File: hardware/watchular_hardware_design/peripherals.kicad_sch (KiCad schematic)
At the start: 43 parts, among them Q1 BSS123, Q2 BSS123, Q3 BSS123, Q4 BSS123

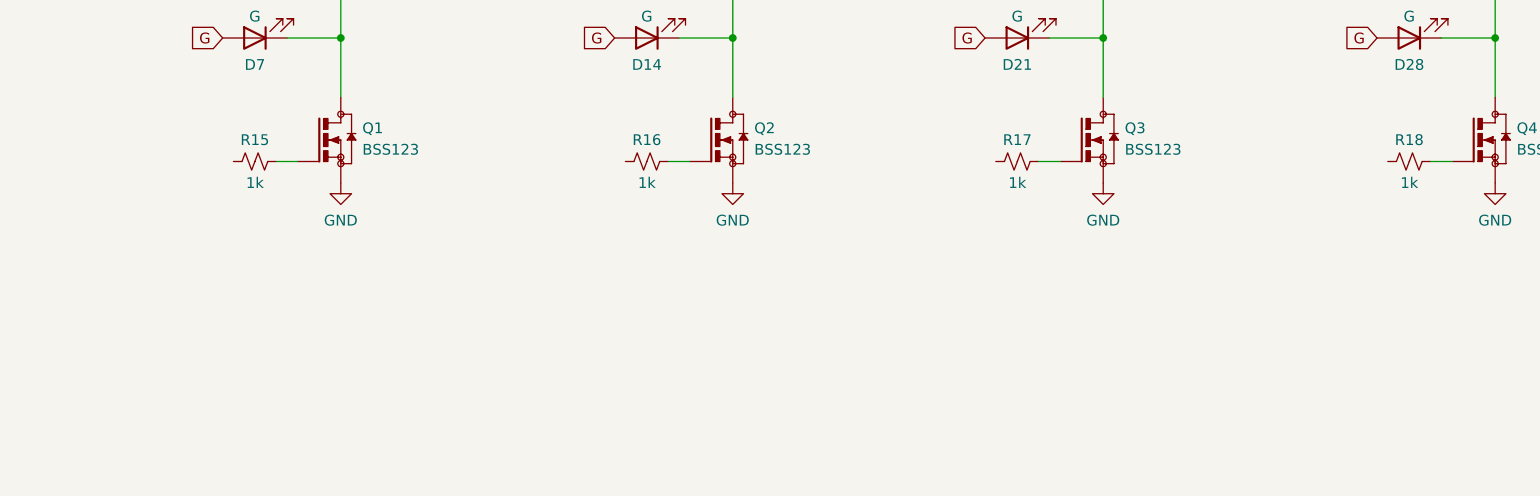
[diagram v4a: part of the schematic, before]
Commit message: Imported button library.
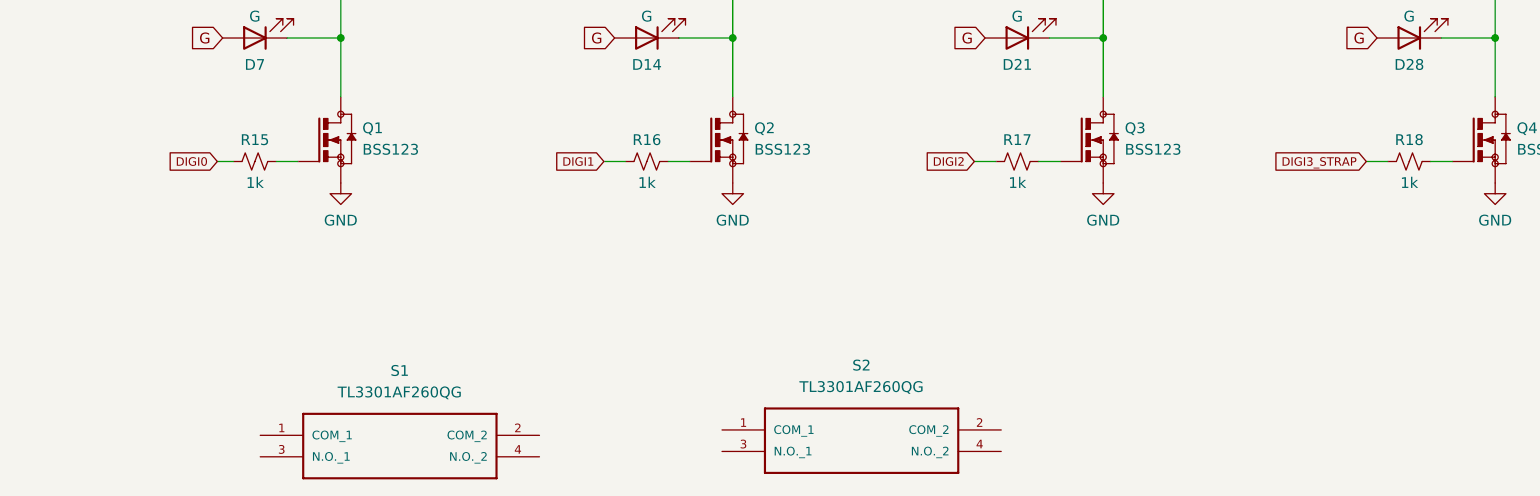
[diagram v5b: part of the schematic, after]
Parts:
- added S1, S2: TL3301AF260QG, switch-TL3301AF260QG:TL3301AF260QG, symbol TL3301AF260QG:TL3301AF260QG
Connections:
- net DIGI0: now reaches R15.1
- net DIGI2: now reaches R17.1
- net DIGI3_STRAP: now reaches R18.1
- net DIGI1: now reaches R16.1
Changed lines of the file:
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@@
+    (stroke (width 0) (type default) (color 0 0 0 0))
+  )
+  (wire (pts (xy 211.455 85.725) (xy 213.995 85.725))
     (stroke (width 0) (type default) (color 0 0 0 0))
   )
@@
     (stroke (width 0) (type default) (color 0 0 0 0))
   )
+  (wire (pts (xy 75.565 85.725) (xy 77.47 85.725))
+    (stroke (width 0) (type default) (color 0 0 0 0))
+  )
   (wire (pts (xy 130.175 45.085) (xy 136.525 45.085))
     (stroke (width 0) (type default) (color 0 0 0 0))
@@
     (stroke (width 0) (type default) (color 0 0 0 0))
   )
+  (wire (pts (xy 165.1 85.725) (xy 167.64 85.725))
+    (stroke (width 0) (type default) (color 0 0 0 0))
+  )
   (wire (pts (xy 136.525 62.865) (xy 136.525 71.12))
     (stroke (width 0) (type default) (color 0 0 0 0))
@@
   )
   (wire (pts (xy 172.72 85.725) (xy 175.26 85.725))
+    (stroke (width 0) (type default) (color 0 0 0 0))
+  )
+  (wire (pts (xy 121.285 85.725) (xy 123.825 85.725))
     (stroke (width 0) (type default) (color 0 0 0 0))
   )
@@
     )
   )
+  (global_label "DIGI3_STRAP" (shape input) (at 211.455 85.725 180) (fields_autoplaced)
+    (effects (font (size 1 1)) (justify right))
+    (property "Intersheet References" "${INTERSHEET_REFS}" (id 0) (at 200.3169 85.7875 0)
+      (effects (font (size 1 1)) (justify right) hide)
+    )
+  )
   (global_label "E" (shape input) (at 122.555 53.975 180) (fields_autoplaced)
     (effects (font (size 1.27 1.27)) (justify right))
@@
     )
   )
+  (global_label "DIGI2" (shape input) (at 165.1 85.725 180) (fields_autoplaced)
+    (effects (font (size 1 1)) (justify right))
+    (property "Intersheet References" "${INTERSHEET_REFS}" (id 0) (at 159.2952 85.7875 0)
+      (effects (font (size 1 1)) (justify right) hide)
+    )
+  )
   (global_label "F" (shape input) (at 166.37 62.865 180) (fields_autoplaced)
     (effects (font (size 1.27 1.27)) (justify right))
@@
     )
   )
+  (global_label "DIGI0" (shape input) (at 75.565 85.725 180) (fields_autoplaced)
+    (effects (font (size 1 1)) (justify right))
+    (property "Intersheet References" "${INTERSHEET_REFS}" (id 0) (at 69.7602 85.7875 0)
+      (effects (font (size 1 1)) (justify right) hide)
+    )
+  )
   (global_label "F_MCU" (shape input) (at 34.29 62.865 0) (fields_autoplaced)
     (effects (font (size 1 1)) (justify left))
@@
     (property "Intersheet References" "${INTERSHEET_REFS}" (id 0) (at 118.8719 36.2744 0)
       (effects (font (size 1.27 1.27)) (justify right) hide)
+    )
+  )
+  (global_label "DIGI1" (shape input) (at 121.285 85.725 180) (fields_autoplaced)
+    (effects (font (size 1 1)) (justify right))
+    (property "Intersheet References" "${INTERSHEET_REFS}" (id 0) (at 115.4802 85.7875 0)
+      (effects (font (size 1 1)) (justify right) hide)
     )
   )
@@
     (pin "2")
   )
+  (symbol (lib_id "TL3301AF260QG:TL3301AF260QG") (at 135.255 117.475 0) (unit 1)
+    (in_bom yes) (on_board yes) (fields_autoplaced)
+    (property "Reference" "S2" (id 0) (at 151.765 109.855 0))
+    (property "Value" "TL3301AF260QG" (id 1) (at 151.765 112.395 0))
+    (property "Footprint" "switch-TL3301AF260QG:TL3301AF260QG" (id 2) (at 135.255 117.475 0)
+      (effects (font (size 1.27 1.27)) (justify left bottom) hide)
+    )
+    (property "Datasheet" "" (id 3) (at 135.255 117.475 0)
+      (effects (font (size 1.27 1.27)) (justify left bottom) hide)
+    )
+    (property "HEIGHT" "7mm" (id 4) (at 135.255 117.475 0)
+      (effects (font (size 1.27 1.27)) (justify left bottom) hide)
+    )
+    (property "MOUSER_PART_NUMBER" "612-TL3301AF2" (id 5) (at 135.255 117.475 0)
+      (effects (font (size 1.27 1.27)) (justify left bottom) hide)
+    )
+    (property "DESCRIPTION" "E-SWITCH - TL3301AF260QG - SWITCH, TACTILE SPST 50mA, SMD GULL WING" (id 6) (at 135.255 117.475 0)
+      (effects (font (size 1.27 1.27)) (justify left bottom) hide)
+    )
+    (property "MOUSER_PRICE-STOCK" "https://www.mouser.com/Search/Refine.aspx?Keyword=612-TL3301AF2" (id 7) (at 135.255 117.475 0)
+      (effects (font (size 1.27 1.27)) (justify left bottom) hide)
+    )
+    (property "MANUFACTURER_NAME" "E-Switch" (id 8) (at 135.255 117.475 0)
+      (effects (font (size 1.27 1.27)) (justify left bottom) hide)
+    )
+    (property "MANUFACTURER_PART_NUMBER" "TL3301AF260QG" (id 9) (at 135.255 117.475 0)
+      (effects (font (size 1.27 1.27)) (justify left bottom) hide)
+    )
+    (pin "1")
+    (pin "2")
+    (pin "3")
+    (pin "4")
+  )
   (symbol (lib_id "power:GND") (at 226.695 88.265 0) (unit 1)
     (in_bom yes) (on_board yes) (fields_autoplaced)
@@
     (pin "1")
   )
+  (symbol (lib_id "TL3301AF260QG:TL3301AF260QG") (at 80.645 118.11 0) (unit 1)
+    (in_bom yes) (on_board yes) (fields_autoplaced)
+    (property "Reference" "S1" (id 0) (at 97.155 110.49 0))
+    (property "Value" "TL3301AF260QG" (id 1) (at 97.155 113.03 0))
+    (property "Footprint" "switch-TL3301AF260QG:TL3301AF260QG" (id 2) (at 80.645 118.11 0)
+      (effects (font (size 1.27 1.27)) (justify left bottom) hide)
+    )
+    (property "Datasheet" "" (id 3) (at 80.645 118.11 0)
+      (effects (font (size 1.27 1.27)) (justify left bottom) hide)
+    )
+    (property "HEIGHT" "7mm" (id 4) (at 80.645 118.11 0)
+      (effects (font (size 1.27 1.27)) (justify left bottom) hide)
+    )
+    (property "MOUSER_PART_NUMBER" "612-TL3301AF2" (id 5) (at 80.645 118.11 0)
+      (effects (font (size 1.27 1.27)) (justify left bottom) hide)
+    )
+    (property "DESCRIPTION" "E-SWITCH - TL3301AF260QG - SWITCH, TACTILE SPST 50mA, SMD GULL WING" (id 6) (at 80.645 118.11 0)
+      (effects (font (size 1.27 1.27)) (justify left bottom) hide)
+    )
+    (property "MOUSER_PRICE-STOCK" "https://www.mouser.com/Search/Refine.aspx?Keyword=612-TL3301AF2" (id 7) (at 80.645 118.11 0)
+      (effects (font (size 1.27 1.27)) (justify left bottom) hide)
+    )
+    (property "MANUFACTURER_NAME" "E-Switch" (id 8) (at 80.645 118.11 0)
+      (effects (font (size 1.27 1.27)) (justify left bottom) hide)
+    )
+    (property "MANUFACTURER_PART_NUMBER" "TL3301AF260QG" (id 9) (at 80.645 118.11 0)
+      (effects (font (size 1.27 1.27)) (justify left bottom) hide)
+    )
+    (pin "1")
+    (pin "2")
+    (pin "3")
+    (pin "4")
+  )
   (symbol (lib_id "BSS123:BSS123") (at 136.525 83.185 0) (unit 1)

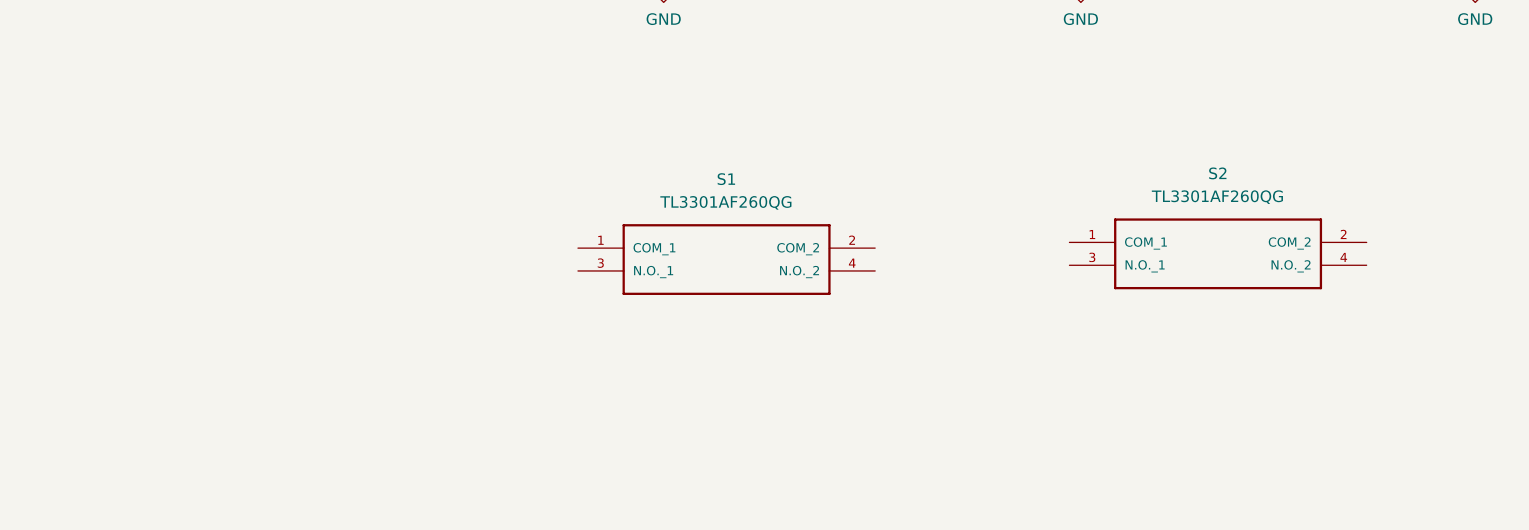
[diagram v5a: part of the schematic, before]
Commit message: Connected buttons.
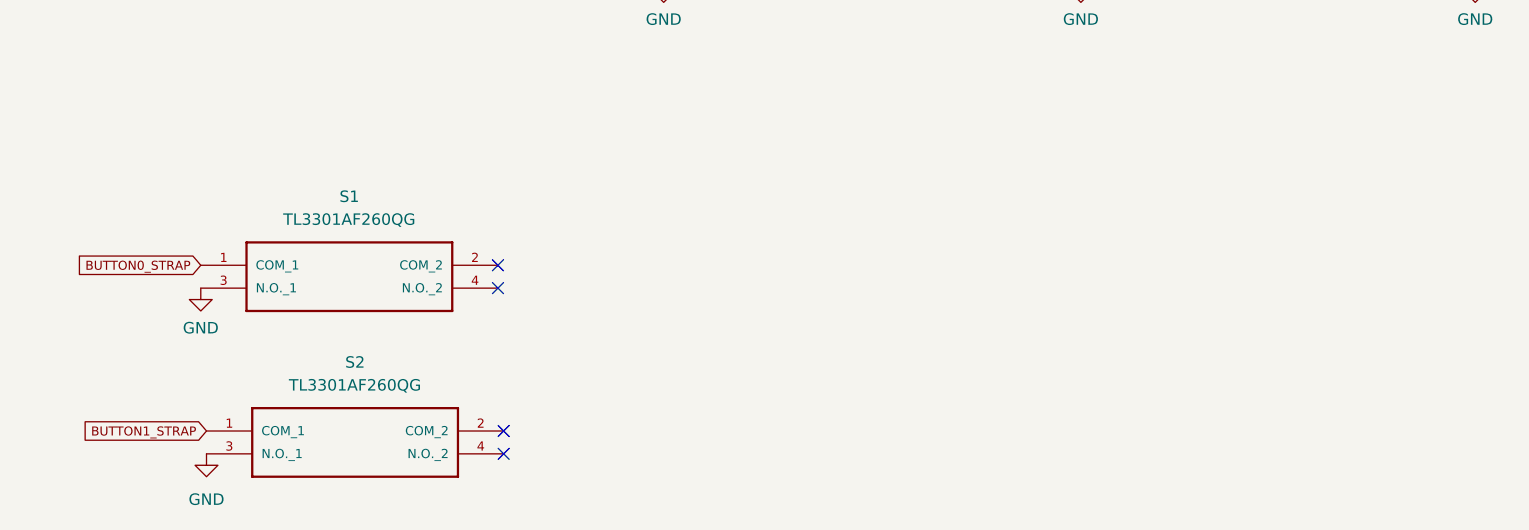
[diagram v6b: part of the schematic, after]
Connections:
- net GND: now also S1.3 (N.O._1), S2.3 (N.O._1)
- net BUTTON1_STRAP: now reaches S2.1 (COM_1)
- net BUTTON0_STRAP: now reaches S1.1 (COM_1)
- no-connect marks 0 -> 4
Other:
- moved on the sheet: S1, S2
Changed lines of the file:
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@@
   (junction (at 136.525 27.94) (diameter 0) (color 0 0 0 0)
   )
+  (no_connect (at 71.755 120.015))
+  (no_connect (at 71.755 122.555))
+  (no_connect (at 72.39 138.43))
+  (no_connect (at 72.39 140.97))
   (wire (pts (xy 220.345 45.085) (xy 226.695 45.085))
     (stroke (width 0) (type default) (color 0 0 0 0))
@@
     )
   )
+  (global_label "BUTTON1_STRAP" (shape input) (at 39.37 138.43 180) (fields_autoplaced)
+    (effects (font (size 1 1)) (justify right))
+    (property "Intersheet References" "${INTERSHEET_REFS}" (id 0) (at 25.5176 138.4925 0)
+      (effects (font (size 1 1)) (justify right) hide)
+    )
+  )
   (global_label "G" (shape input) (at 166.37 71.12 180) (fields_autoplaced)
     (effects (font (size 1.27 1.27)) (justify right))
     (property "Intersheet References" "${INTERSHEET_REFS}" (id 0) (at 162.6869 71.1994 0)
       (effects (font (size 1.27 1.27)) (justify right) hide)
+    )
+  )
+  (global_label "BUTTON0_STRAP" (shape input) (at 38.735 120.015 180) (fields_autoplaced)
+    (effects (font (size 1 1)) (justify right))
+    (property "Intersheet References" "${INTERSHEET_REFS}" (id 0) (at 24.8826 120.0775 0)
+      (effects (font (size 1 1)) (justify right) hide)
     )
   )
@@
     (pin "2")
   )
+  (symbol (lib_id "power:GND") (at 38.735 122.555 0) (unit 1)
+    (in_bom yes) (on_board yes) (fields_autoplaced)
+    (property "Reference" "#PWR0101" (id 0) (at 38.735 128.905 0)
+      (effects (font (size 1.27 1.27)) hide)
+    )
+    (property "Value" "GND" (id 1) (at 38.735 127 0))
+    (property "Footprint" "" (id 2) (at 38.735 122.555 0)
+      (effects (font (size 1.27 1.27)) hide)
+    )
+    (property "Datasheet" "" (id 3) (at 38.735 122.555 0)
+      (effects (font (size 1.27 1.27)) hide)
+    )
+    (pin "1")
+  )
   (symbol (lib_id "Device:LED") (at 126.365 27.94 180) (unit 1)
     (in_bom yes) (on_board yes)
@@
     (pin "3")
   )
+  (symbol (lib_id "power:GND") (at 39.37 140.97 0) (unit 1)
+    (in_bom yes) (on_board yes) (fields_autoplaced)
+    (property "Reference" "#PWR0102" (id 0) (at 39.37 147.32 0)
+      (effects (font (size 1.27 1.27)) hide)
+    )
+    (property "Value" "GND" (id 1) (at 39.37 146.05 0))
+    (property "Footprint" "" (id 2) (at 39.37 140.97 0)
+      (effects (font (size 1.27 1.27)) hide)
+    )
+    (property "Datasheet" "" (id 3) (at 39.37 140.97 0)
+      (effects (font (size 1.27 1.27)) hide)
+    )
+    (pin "1")
+  )
   (symbol (lib_id "Device:LED") (at 216.535 27.94 180) (unit 1)
     (in_bom yes) (on_board yes)
@@
     (pin "2")
   )
-  (symbol (lib_id "TL3301AF260QG:TL3301AF260QG") (at 135.255 117.475 0) (unit 1)
-    (in_bom yes) (on_board yes) (fields_autoplaced)
-    (property "Reference" "S2" (id 0) (at 151.765 109.855 0))
-    (property "Value" "TL3301AF260QG" (id 1) (at 151.765 112.395 0))
-    (property "Footprint" "switch-TL3301AF260QG:TL3301AF260QG" (id 2) (at 135.255 117.475 0)
-      (effects (font (size 1.27 1.27)) (justify left bottom) hide)
-    )
-    (property "Datasheet" "" (id 3) (at 135.255 117.475 0)
-      (effects (font (size 1.27 1.27)) (justify left bottom) hide)
-    )
-    (property "HEIGHT" "7mm" (id 4) (at 135.255 117.475 0)
-      (effects (font (size 1.27 1.27)) (justify left bottom) hide)
-    )
-    (property "MOUSER_PART_NUMBER" "612-TL3301AF2" (id 5) (at 135.255 117.475 0)
-      (effects (font (size 1.27 1.27)) (justify left bottom) hide)
-    )
-    (property "DESCRIPTION" "E-SWITCH - TL3301AF260QG - SWITCH, TACTILE SPST 50mA, SMD GULL WING" (id 6) (at 135.255 117.475 0)
-      (effects (font (size 1.27 1.27)) (justify left bottom) hide)
-    )
-    (property "MOUSER_PRICE-STOCK" "https://www.mouser.com/Search/Refine.aspx?Keyword=612-TL3301AF2" (id 7) (at 135.255 117.475 0)
-      (effects (font (size 1.27 1.27)) (justify left bottom) hide)
-    )
-    (property "MANUFACTURER_NAME" "E-Switch" (id 8) (at 135.255 117.475 0)
-      (effects (font (size 1.27 1.27)) (justify left bottom) hide)
-    )
-    (property "MANUFACTURER_PART_NUMBER" "TL3301AF260QG" (id 9) (at 135.255 117.475 0)
+  (symbol (lib_id "TL3301AF260QG:TL3301AF260QG") (at 39.37 138.43 0) (unit 1)
+    (in_bom yes) (on_board yes) (fields_autoplaced)
+    (property "Reference" "S2" (id 0) (at 55.88 130.81 0))
+    (property "Value" "TL3301AF260QG" (id 1) (at 55.88 133.35 0))
+    (property "Footprint" "switch-TL3301AF260QG:TL3301AF260QG" (id 2) (at 39.37 138.43 0)
+      (effects (font (size 1.27 1.27)) (justify left bottom) hide)
+    )
+    (property "Datasheet" "" (id 3) (at 39.37 138.43 0)
+      (effects (font (size 1.27 1.27)) (justify left bottom) hide)
+    )
+    (property "HEIGHT" "7mm" (id 4) (at 39.37 138.43 0)
+      (effects (font (size 1.27 1.27)) (justify left bottom) hide)
+    )
+    (property "MOUSER_PART_NUMBER" "612-TL3301AF2" (id 5) (at 39.37 138.43 0)
+      (effects (font (size 1.27 1.27)) (justify left bottom) hide)
+    )
+    (property "DESCRIPTION" "E-SWITCH - TL3301AF260QG - SWITCH, TACTILE SPST 50mA, SMD GULL WING" (id 6) (at 39.37 138.43 0)
+      (effects (font (size 1.27 1.27)) (justify left bottom) hide)
+    )
+    (property "MOUSER_PRICE-STOCK" "https://www.mouser.com/Search/Refine.aspx?Keyword=612-TL3301AF2" (id 7) (at 39.37 138.43 0)
+      (effects (font (size 1.27 1.27)) (justify left bottom) hide)
+    )
+    (property "MANUFACTURER_NAME" "E-Switch" (id 8) (at 39.37 138.43 0)
+      (effects (font (size 1.27 1.27)) (justify left bottom) hide)
+    )
+    (property "MANUFACTURER_PART_NUMBER" "TL3301AF260QG" (id 9) (at 39.37 138.43 0)
       (effects (font (size 1.27 1.27)) (justify left bottom) hide)
     )
@@
     (pin "1")
   )
-  (symbol (lib_id "TL3301AF260QG:TL3301AF260QG") (at 80.645 118.11 0) (unit 1)
-    (in_bom yes) (on_board yes) (fields_autoplaced)
-    (property "Reference" "S1" (id 0) (at 97.155 110.49 0))
-    (property "Value" "TL3301AF260QG" (id 1) (at 97.155 113.03 0))
-    (property "Footprint" "switch-TL3301AF260QG:TL3301AF260QG" (id 2) (at 80.645 118.11 0)
-      (effects (font (size 1.27 1.27)) (justify left bottom) hide)
-    )
-    (property "Datasheet" "" (id 3) (at 80.645 118.11 0)
-      (effects (font (size 1.27 1.27)) (justify left bottom) hide)
-    )
-    (property "HEIGHT" "7mm" (id 4) (at 80.645 118.11 0)
-      (effects (font (size 1.27 1.27)) (justify left bottom) hide)
-    )
-    (property "MOUSER_PART_NUMBER" "612-TL3301AF2" (id 5) (at 80.645 118.11 0)
-      (effects (font (size 1.27 1.27)) (justify left bottom) hide)
-    )
-    (property "DESCRIPTION" "E-SWITCH - TL3301AF260QG - SWITCH, TACTILE SPST 50mA, SMD GULL WING" (id 6) (at 80.645 118.11 0)
-      (effects (font (size 1.27 1.27)) (justify left bottom) hide)
-    )
-    (property "MOUSER_PRICE-STOCK" "https://www.mouser.com/Search/Refine.aspx?Keyword=612-TL3301AF2" (id 7) (at 80.645 118.11 0)
-      (effects (font (size 1.27 1.27)) (justify left bottom) hide)
-    )
-    (property "MANUFACTURER_NAME" "E-Switch" (id 8) (at 80.645 118.11 0)
-      (effects (font (size 1.27 1.27)) (justify left bottom) hide)
-    )
-    (property "MANUFACTURER_PART_NUMBER" "TL3301AF260QG" (id 9) (at 80.645 118.11 0)
-      (effects (font (size 1.27 1.27)) (justify left bottom) hide)
-    )
+  (symbol (lib_id "TL3301AF260QG:TL3301AF260QG") (at 38.735 120.015 0) (unit 1)
+    (in_bom yes) (on_board yes) (fields_autoplaced)
+    (property "Reference" "S1" (id 0) (at 55.245 112.395 0))
+    (property "Value" "TL3301AF260QG" (id 1) (at 55.245 114.935 0))
+    (property "Footprint" "switch-TL3301AF260QG:TL3301AF260QG" (id 2) (at 38.735 120.015 0)
+      (effects (font (size 1.27 1.27)) (justify left bottom) hide)
+    )
+    (property "Datasheet" "" (id 3) (at 38.735 120.015 0)
+      (effects (font (size 1.27 1.27)) (justify left bottom) hide)
+    )
+    (property "HEIGHT" "7mm" (id 4) (at 38.735 120.015 0)
+      (effects (font (size 1.27 1.27)) (justify left bottom) hide)
+    )
+    (property "MOUSER_PART_NUMBER" "612-TL3301AF2" (id 5) (at 38.735 120.015 0)
+      (effects (font (size 1.27 1.27)) (justify left bottom) hide)
+    )
+    (property "DESCRIPTION" "E-SWITCH - TL3301AF260QG - SWITCH, TACTILE SPST 50mA, SMD GULL WING" (id 6) (at 38.735 120.015 0)
+      (effects (font (size 1.27 1.27)) (justify left bottom) hide)
+    )
+    (property "MOUSER_PRICE-STOCK" "https://www.mouser.com/Search/Refine.aspx?Keyword=612-TL3301AF2" (id 7) (at 38.735 120.015 0)
+      (effects (font (size 1.27 1.27)) (justify left bottom) hide)
+    )
+    (property "MANUFACTURER_NAME" "E-Switch" (id 8) (at 38.735 120.015 0)
+      (effects (font (size 1.27 1.27)) (justify left bottom) hide)
+    )
+    (property "MANUFACTURER_PART_NUMBER" "TL3301AF260QG" (id 9) (at 38.735 120.015 0)
+      (effects (font (size 1.27 1.27)) (justify left bottom) hide)
+    )
